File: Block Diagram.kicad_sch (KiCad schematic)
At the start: 0 parts

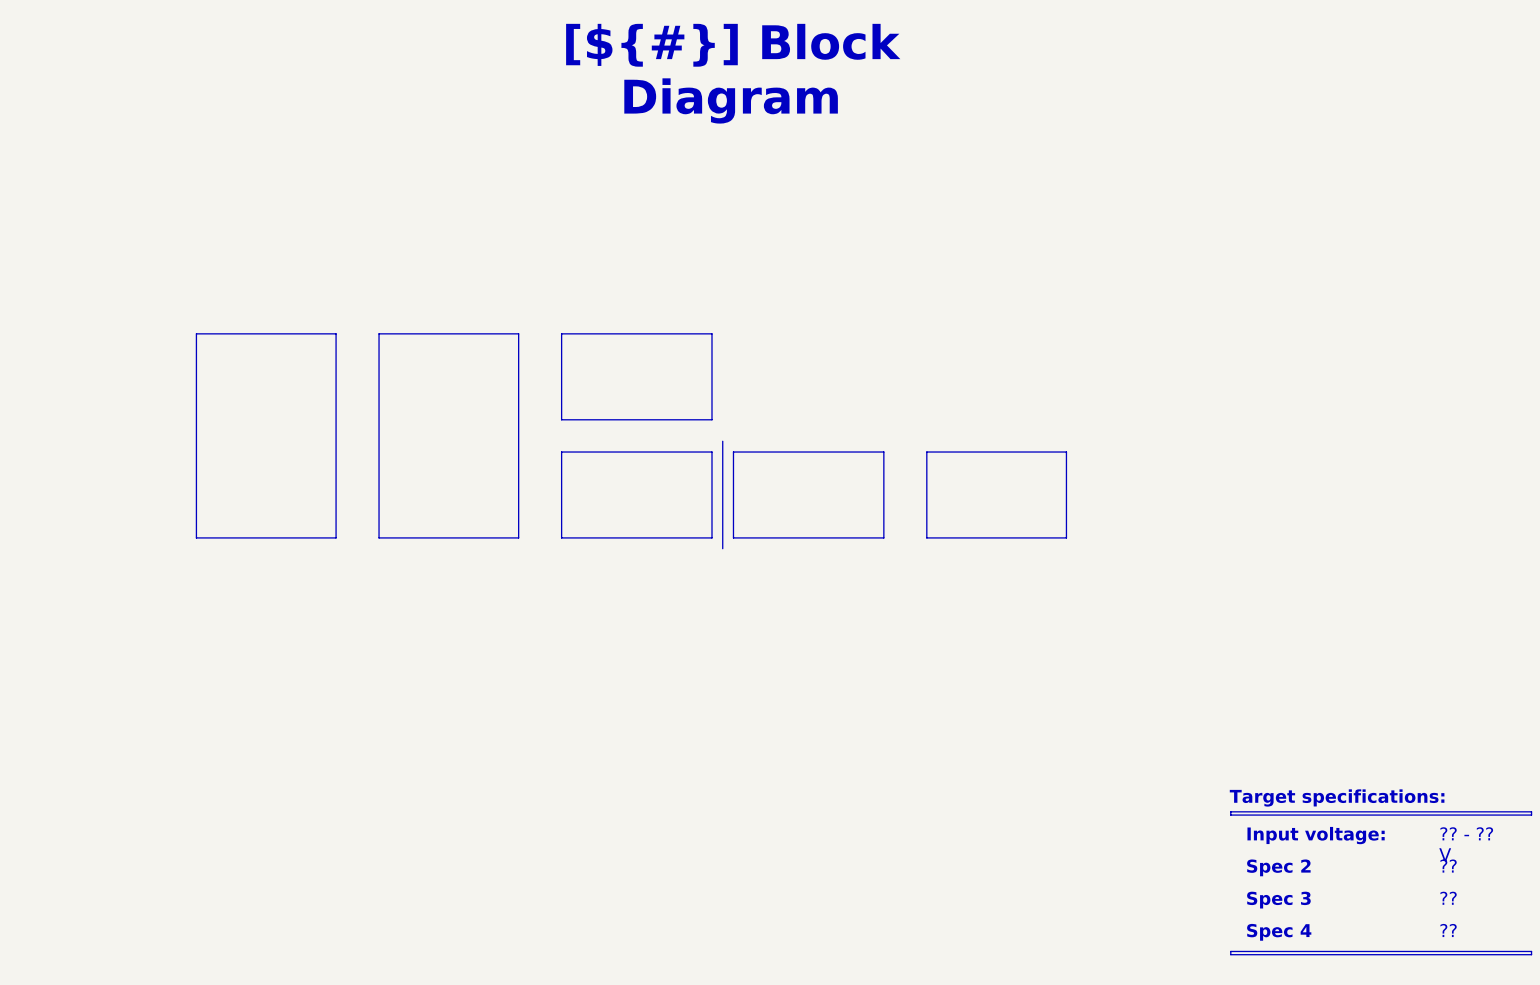
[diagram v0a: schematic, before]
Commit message: documentation update / block diagram
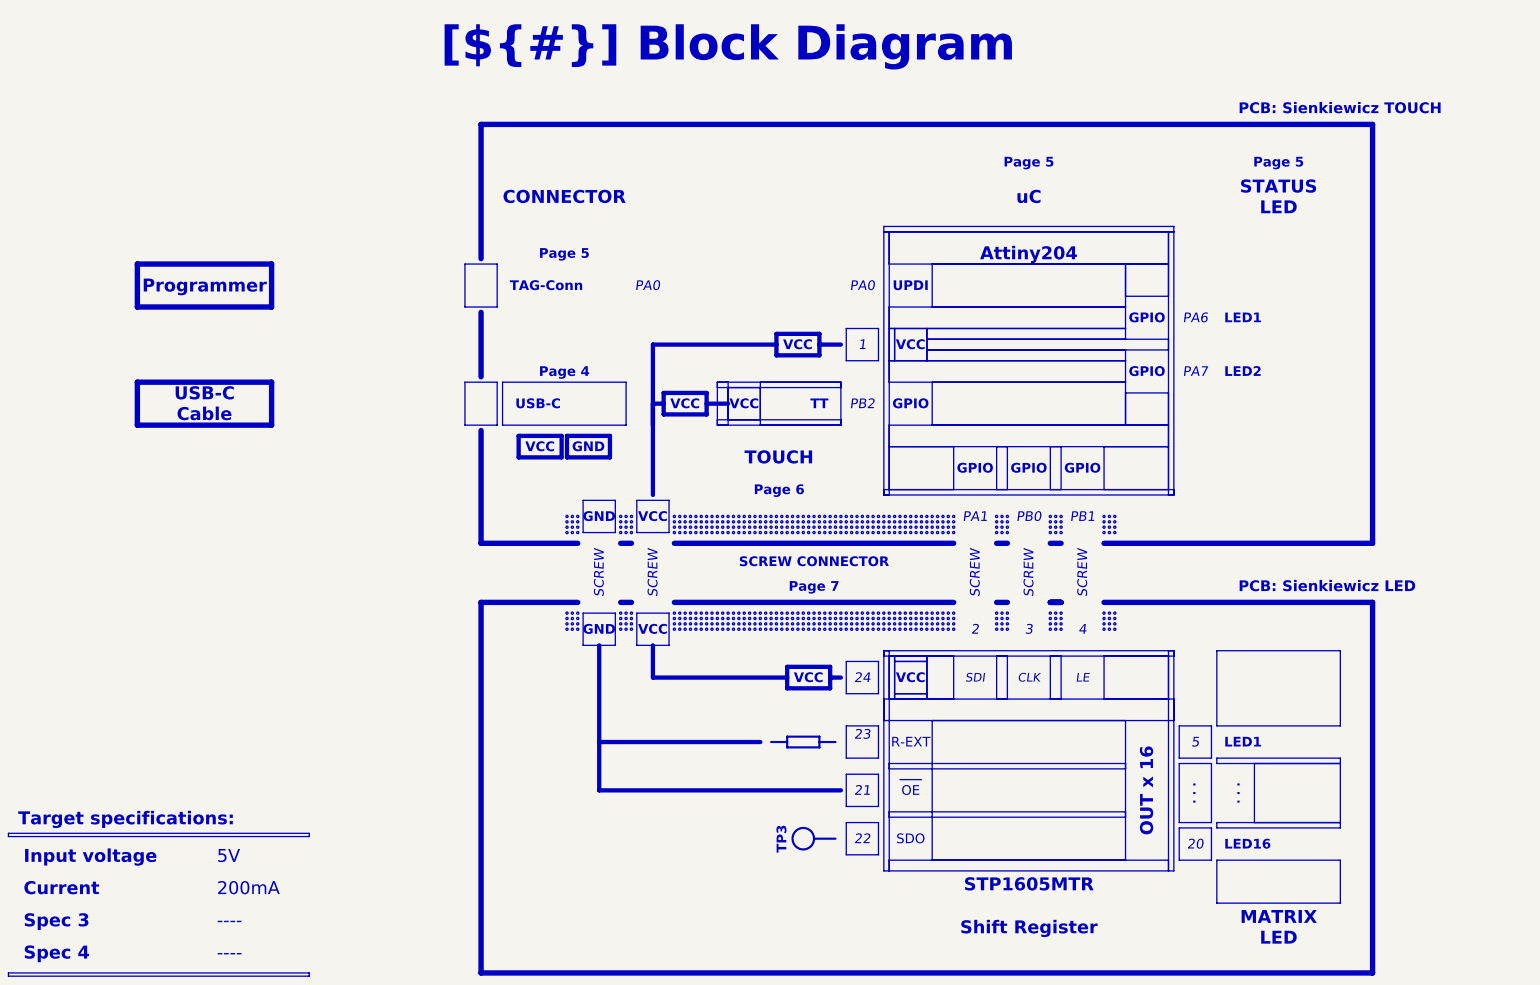
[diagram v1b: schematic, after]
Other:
- note added: "PCB: Sienkiewicz LED"
- note added: "PCB: Sienkiewicz TOUCH"
